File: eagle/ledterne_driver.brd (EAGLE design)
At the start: 100 x 80 mm, 1 part, among them IC1 MEGA8-AI

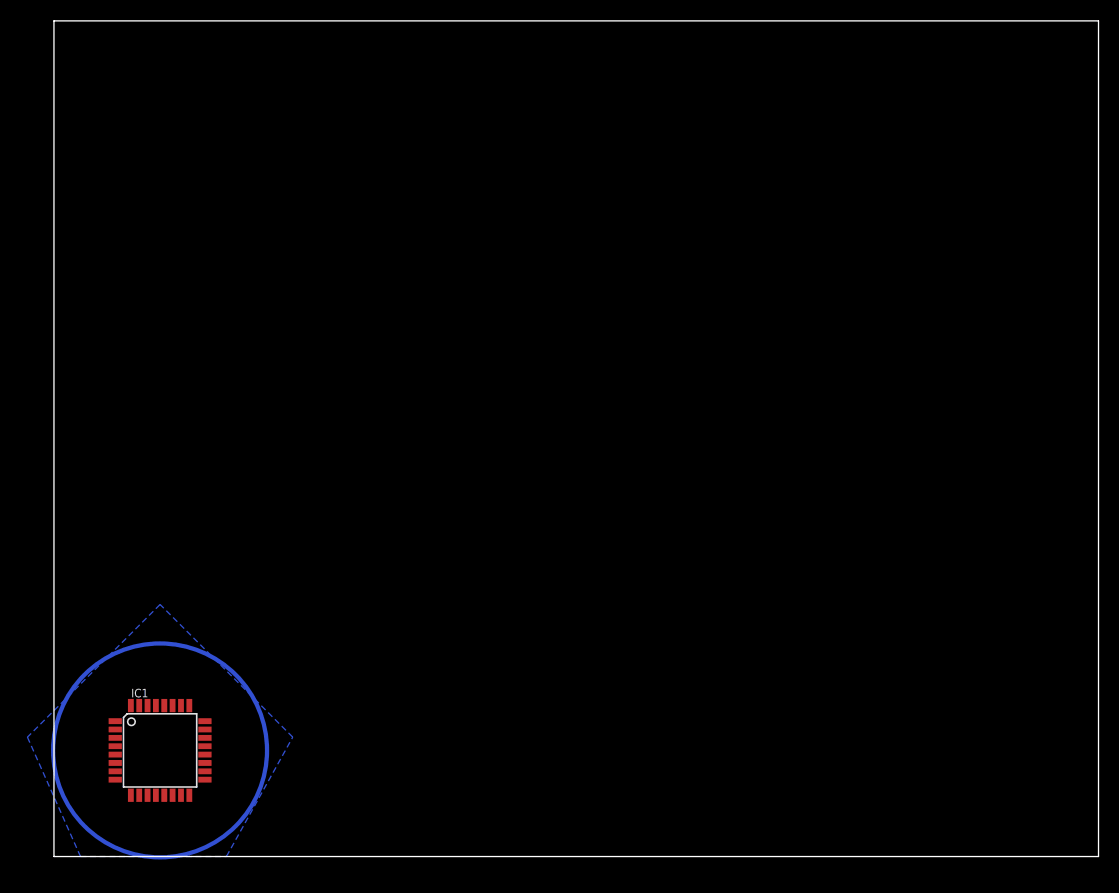
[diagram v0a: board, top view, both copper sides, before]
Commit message: Change driver board to match the display board size
5 display boards will be arranged in an upright position forming
a cylinder with a pentagonal base. The driver board is a pentagon
that then acts as sort of lid for this cylinder.
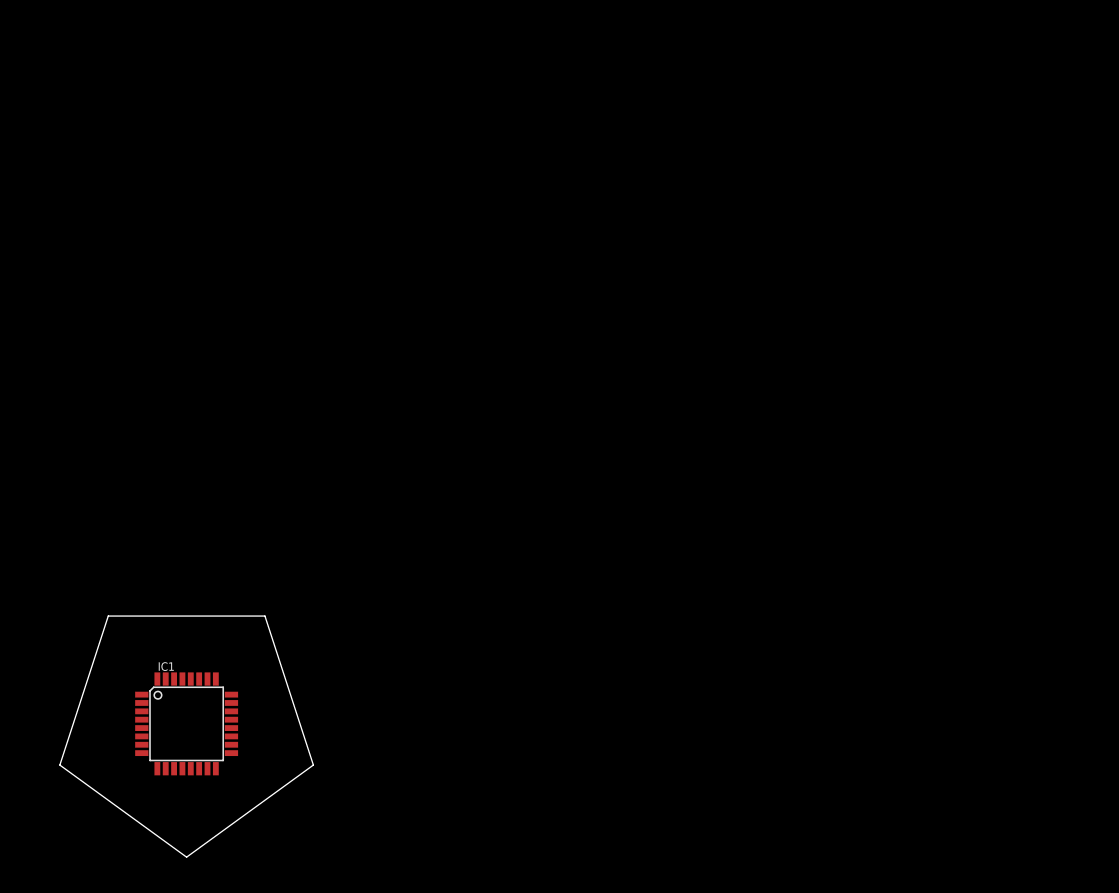
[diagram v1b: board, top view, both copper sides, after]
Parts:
- moved IC1 3.59 mm to (12.7, 12.7)
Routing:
- removed copper zone on layer 16, net N$1
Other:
- board size 100 x 80 mm -> 24.3 x 23.1 mm
- board text added: "15 mm"
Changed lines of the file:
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@@
 <layer number="45" name="Holes" color="7" fill="1" visible="no" active="yes"/>
 <layer number="46" name="Milling" color="3" fill="1" visible="no" active="yes"/>
-<layer number="47" name="Measures" color="7" fill="1" visible="no" active="yes"/>
+<layer number="47" name="Measures" color="7" fill="1" visible="yes" active="yes"/>
 <layer number="48" name="Document" color="7" fill="1" visible="yes" active="yes"/>
 <layer number="49" name="Reference" color="7" fill="1" visible="yes" active="yes"/>
@@
 <board>
 <plain>
-<wire x1="0" y1="0" x2="100" y2="0" width="0" layer="20"/>
-<wire x1="100" y1="0" x2="100" y2="80" width="0" layer="20"/>
-<wire x1="100" y1="80" x2="0" y2="80" width="0" layer="20"/>
-<wire x1="0" y1="80" x2="0" y2="0" width="0" layer="20"/>
-<circle x="10.16" y="10.16" radius="10.239065625" width="0.4064" layer="16"/>
+<circle x="12.7" y="12.7" radius="12.76" width="0.1" layer="49"/>
+<wire x1="12.7" y1="-0.06" x2="24.8353" y2="8.757" width="0.1" layer="20"/>
+<wire x1="24.8353" y1="8.757" x2="20.2" y2="23.0229" width="0.1" layer="20"/>
+<wire x1="20.2" y1="23.0229" x2="5.2" y2="23.0229" width="0.1" layer="20"/>
+<wire x1="5.2" y1="23.0229" x2="0.5647" y2="8.757" width="0.1" layer="20"/>
+<wire x1="0.5647" y1="8.757" x2="12.7" y2="-0.06" width="0.1" layer="20"/>
+<wire x1="20.2" y1="27.94" x2="5.2" y2="27.94" width="0.1" layer="47"/>
+<text x="12.7" y="29.21" size="1.778" layer="47" align="center">15 mm</text>
+<wire x1="5.2" y1="29.21" x2="5.2" y2="26.67" width="0.1" layer="47"/>
+<wire x1="20.2" y1="29.21" x2="20.2" y2="26.67" width="0.1" layer="47"/>
 </plain>
 <attributes>
@@
 </autorouter>
 <elements>
-<element name="IC1" library="atmel" package="TQFP32-08" value="MEGA8-AI" x="10.16" y="10.16">
-<attribute name="OC_NEWARK" value="73M8863" x="10.16" y="10.16" size="1.778" layer="27" display="off"/>
-<attribute name="MF" value="" x="10.16" y="10.16" size="1.778" layer="27" display="off"/>
-<attribute name="OC_FARNELL" value="9171371" x="10.16" y="10.16" size="1.778" layer="27" display="off"/>
-<attribute name="MPN" value="ATMEGA8-16AU" x="10.16" y="10.16" size="1.778" layer="27" display="off"/>
+<element name="IC1" library="atmel" package="TQFP32-08" value="MEGA8-AI" x="12.7" y="12.7">
+<attribute name="OC_NEWARK" value="73M8863" x="12.7" y="12.7" size="1.778" layer="27" display="off"/>
+<attribute name="MF" value="" x="12.7" y="12.7" size="1.778" layer="27" display="off"/>
+<attribute name="OC_FARNELL" value="9171371" x="12.7" y="12.7" size="1.778" layer="27" display="off"/>
+<attribute name="MPN" value="ATMEGA8-16AU" x="12.7" y="12.7" size="1.778" layer="27" display="off"/>
 </element>
 </elements>
@@
 <contactref element="IC1" pad="5"/>
 <contactref element="IC1" pad="21"/>
-<wire x1="5.8674" y1="11.36" x2="5.8674" y2="9.76" width="0" layer="19" extent="1-1"/>
-<wire x1="14.4526" y1="10.56" x2="5.8674" y2="9.76" width="0" layer="19" extent="1-1"/>
+<wire x1="8.4074" y1="13.9" x2="8.4074" y2="12.3" width="0" layer="19" extent="1-1"/>
+<wire x1="16.9926" y1="13.1" x2="8.4074" y2="12.3" width="0" layer="19" extent="1-1"/>
 </signal>
 <signal name="VCC">
 <contactref element="IC1" pad="4"/>
 <contactref element="IC1" pad="6"/>
-<wire x1="5.8674" y1="10.56" x2="5.8674" y2="8.96" width="0" layer="19" extent="1-1"/>
+<wire x1="8.4074" y1="13.1" x2="8.4074" y2="11.5" width="0" layer="19" extent="1-1"/>
 </signal>
 <signal name="AVCC">
 <contactref element="IC1" pad="18"/>
 </signal>
-<signal name="N$1">
-<polygon width="0.4064" layer="16">
-<vertex x="2.54" y="0"/>
-<vertex x="16.51" y="0"/>
-<vertex x="22.86" y="11.43"/>
-<vertex x="10.16" y="24.13"/>
-<vertex x="-2.54" y="11.43"/>
-</polygon>
-</signal>
 </signals>

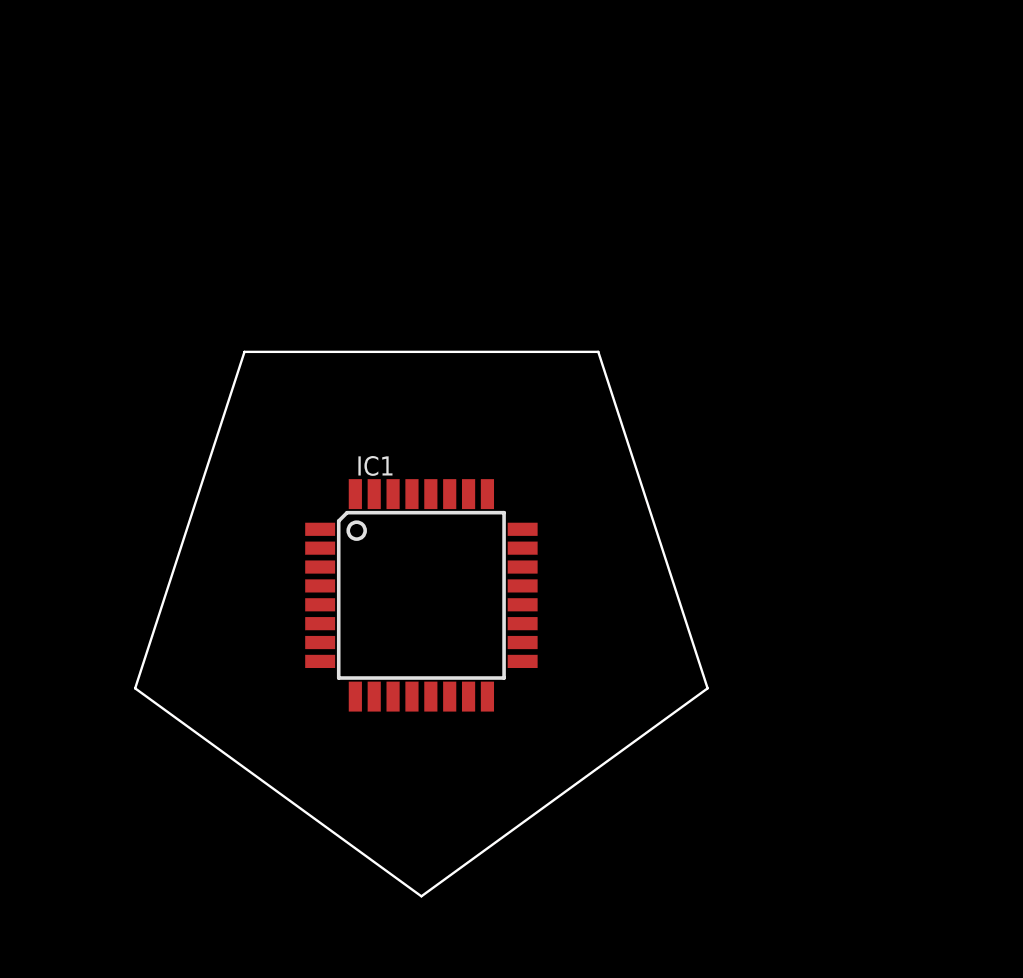
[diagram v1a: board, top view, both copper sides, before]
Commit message: Add connectors to the driver board
These connectors will allow the display boards to attach to the
driver board.

Note that this is just a very rough sketch for demonstrating the
basic idea. The exact placement and type of connectors will have
to be fine-tuned later.
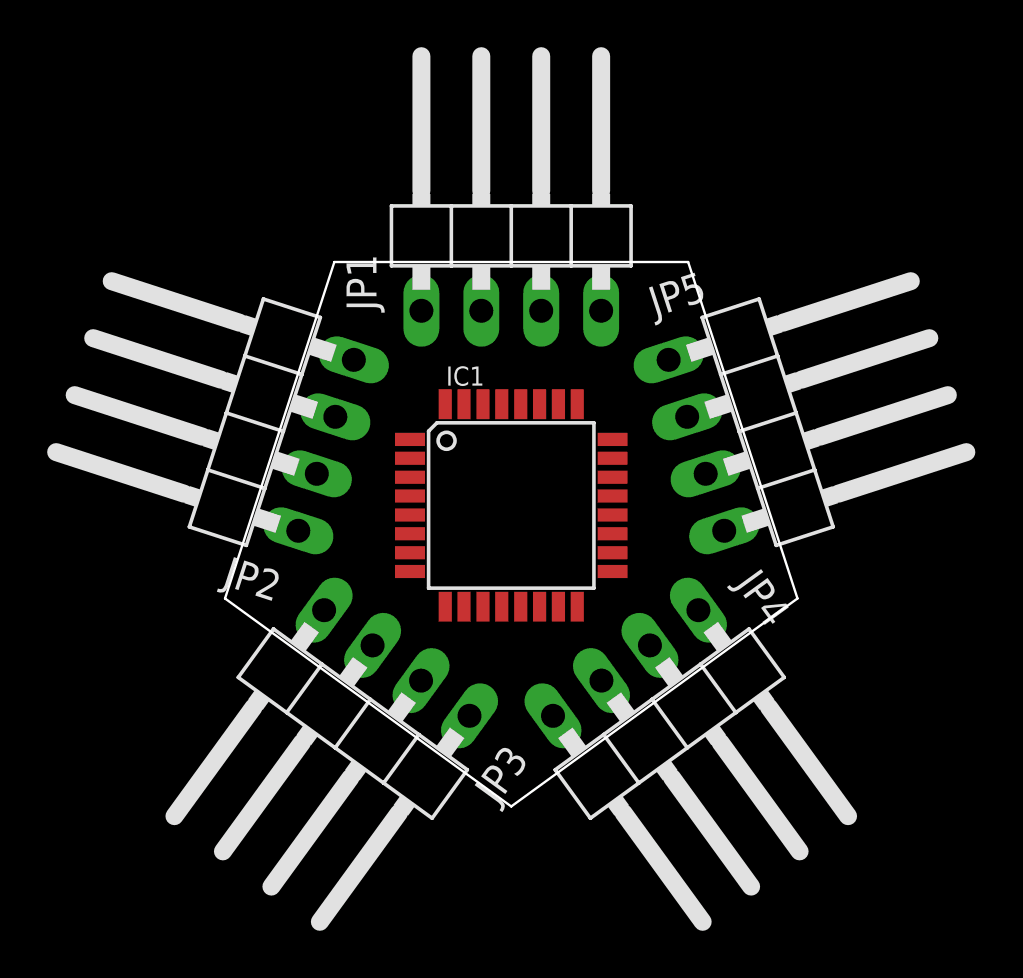
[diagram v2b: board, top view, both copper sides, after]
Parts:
- added JP1, JP2, JP3, JP4, JP5: (no value), pinhead:1X04/90
- moved IC1 5.39 mm to (16.5, 16.5)
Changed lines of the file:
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@@
 <layer number="47" name="Measures" color="7" fill="1" visible="yes" active="yes"/>
 <layer number="48" name="Document" color="7" fill="1" visible="yes" active="yes"/>
-<layer number="49" name="Reference" color="7" fill="1" visible="yes" active="yes"/>
+<layer number="49" name="Reference" color="7" fill="1" visible="no" active="yes"/>
 <layer number="51" name="tDocu" color="7" fill="1" visible="yes" active="yes"/>
 <layer number="52" name="bDocu" color="7" fill="1" visible="yes" active="yes"/>
@@
 <board>
 <plain>
-<circle x="12.7" y="12.7" radius="12.76" width="0.1" layer="49"/>
-<wire x1="12.7" y1="-0.06" x2="24.8353" y2="8.757" width="0.1" layer="20"/>
-<wire x1="24.8353" y1="8.757" x2="20.2" y2="23.0229" width="0.1" layer="20"/>
-<wire x1="20.2" y1="23.0229" x2="5.2" y2="23.0229" width="0.1" layer="20"/>
-<wire x1="5.2" y1="23.0229" x2="0.5647" y2="8.757" width="0.1" layer="20"/>
-<wire x1="0.5647" y1="8.757" x2="12.7" y2="-0.06" width="0.1" layer="20"/>
-<wire x1="20.2" y1="27.94" x2="5.2" y2="27.94" width="0.1" layer="47"/>
-<text x="12.7" y="29.21" size="1.778" layer="47" align="center">15 mm</text>
-<wire x1="5.2" y1="29.21" x2="5.2" y2="26.67" width="0.1" layer="47"/>
-<wire x1="20.2" y1="29.21" x2="20.2" y2="26.67" width="0.1" layer="47"/>
+<circle x="16.51" y="16.51" radius="12.76" width="0.1" layer="49"/>
+<wire x1="16.51" y1="3.75" x2="28.6453" y2="12.567" width="0.1" layer="20"/>
+<wire x1="28.6453" y1="12.567" x2="24.01" y2="26.8329" width="0.1" layer="20"/>
+<wire x1="24.01" y1="26.8329" x2="9.01" y2="26.8329" width="0.1" layer="20"/>
+<wire x1="9.01" y1="26.8329" x2="4.3747" y2="12.567" width="0.1" layer="20"/>
+<wire x1="4.3747" y1="12.567" x2="16.51" y2="3.75" width="0.1" layer="20"/>
+<wire x1="24.01" y1="31.75" x2="9.01" y2="31.75" width="0.1" layer="47"/>
+<text x="16.51" y="33.02" size="1.778" layer="47" align="center">15 mm</text>
+<wire x1="9.01" y1="33.02" x2="9.01" y2="30.48" width="0.1" layer="47"/>
+<wire x1="24.01" y1="33.02" x2="24.01" y2="30.48" width="0.1" layer="47"/>
 </plain>
 <attributes>
@@
 </autorouter>
 <elements>
-<element name="IC1" library="atmel" package="TQFP32-08" value="MEGA8-AI" x="12.7" y="12.7">
-<attribute name="OC_NEWARK" value="73M8863" x="12.7" y="12.7" size="1.778" layer="27" display="off"/>
-<attribute name="MF" value="" x="12.7" y="12.7" size="1.778" layer="27" display="off"/>
-<attribute name="OC_FARNELL" value="9171371" x="12.7" y="12.7" size="1.778" layer="27" display="off"/>
-<attribute name="MPN" value="ATMEGA8-16AU" x="12.7" y="12.7" size="1.778" layer="27" display="off"/>
+<element name="IC1" library="atmel" package="TQFP32-08" value="MEGA8-AI" x="16.51" y="16.51">
+<attribute name="OC_NEWARK" value="73M8863" x="16.51" y="16.51" size="1.778" layer="27" display="off"/>
+<attribute name="MF" value="" x="16.51" y="16.51" size="1.778" layer="27" display="off"/>
+<attribute name="OC_FARNELL" value="9171371" x="16.51" y="16.51" size="1.778" layer="27" display="off"/>
+<attribute name="MPN" value="ATMEGA8-16AU" x="16.51" y="16.51" size="1.778" layer="27" display="off"/>
 </element>
+<element name="JP1" library="pinhead" package="1X04/90" value="" x="16.51" y="28.575"/>
+<element name="JP2" library="pinhead" package="1X04/90" value="" x="5.0355" y="20.238" rot="R72"/>
+<element name="JP3" library="pinhead" package="1X04/90" value="" x="9.4184" y="6.7492" rot="R144"/>
+<element name="JP4" library="pinhead" package="1X04/90" value="" x="23.6016" y="6.7492" rot="R216"/>
+<element name="JP5" library="pinhead" package="1X04/90" value="" x="27.984" y="20.238" rot="R288"/>
 </elements>
 <signals>
@@
 <contactref element="IC1" pad="5"/>
 <contactref element="IC1" pad="21"/>
-<wire x1="8.4074" y1="13.9" x2="8.4074" y2="12.3" width="0" layer="19" extent="1-1"/>
-<wire x1="16.9926" y1="13.1" x2="8.4074" y2="12.3" width="0" layer="19" extent="1-1"/>
+<wire x1="12.2174" y1="17.71" x2="12.2174" y2="16.11" width="0" layer="19" extent="1-1"/>
+<wire x1="20.8026" y1="16.91" x2="12.2174" y2="16.11" width="0" layer="19" extent="1-1"/>
 </signal>
 <signal name="VCC">
 <contactref element="IC1" pad="4"/>
 <contactref element="IC1" pad="6"/>
-<wire x1="8.4074" y1="13.1" x2="8.4074" y2="11.5" width="0" layer="19" extent="1-1"/>
+<wire x1="12.2174" y1="16.91" x2="12.2174" y2="15.31" width="0" layer="19" extent="1-1"/>
 </signal>
 <signal name="AVCC">

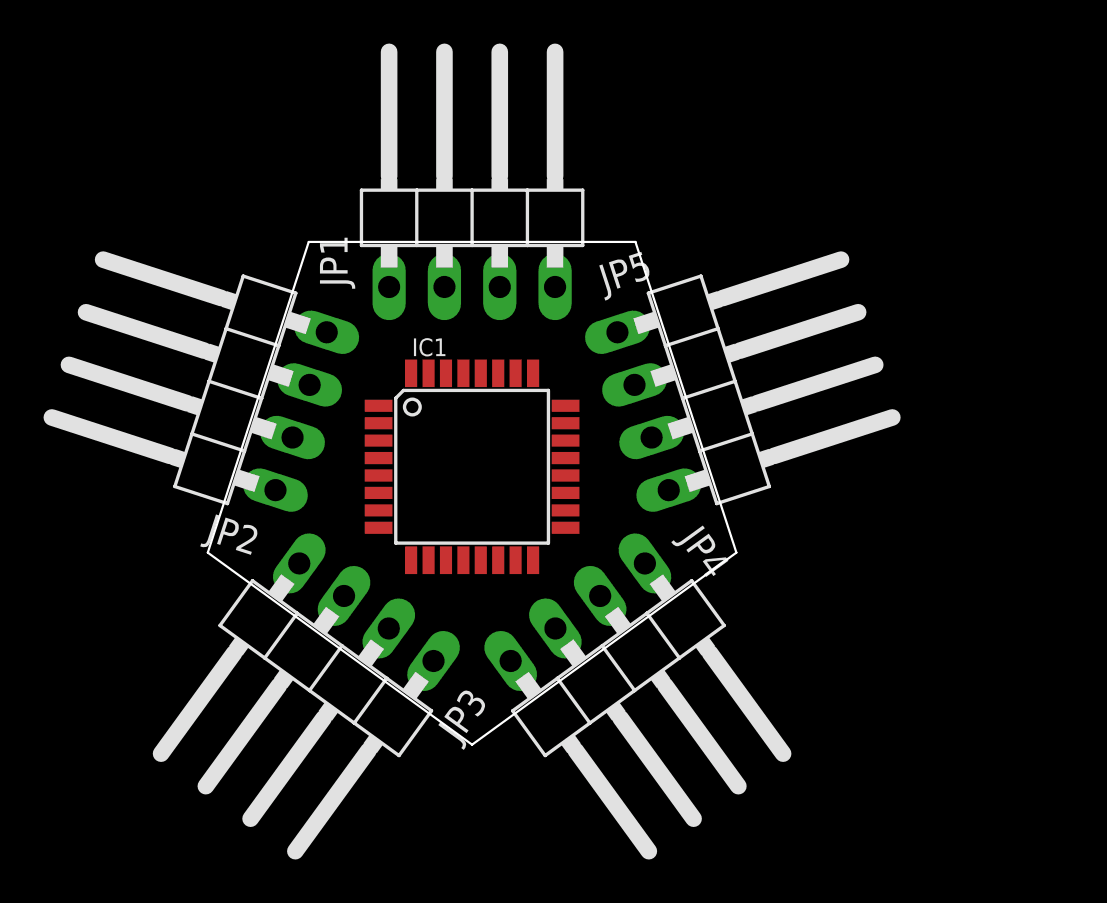
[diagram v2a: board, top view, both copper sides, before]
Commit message: Start connecting the components of the driver.
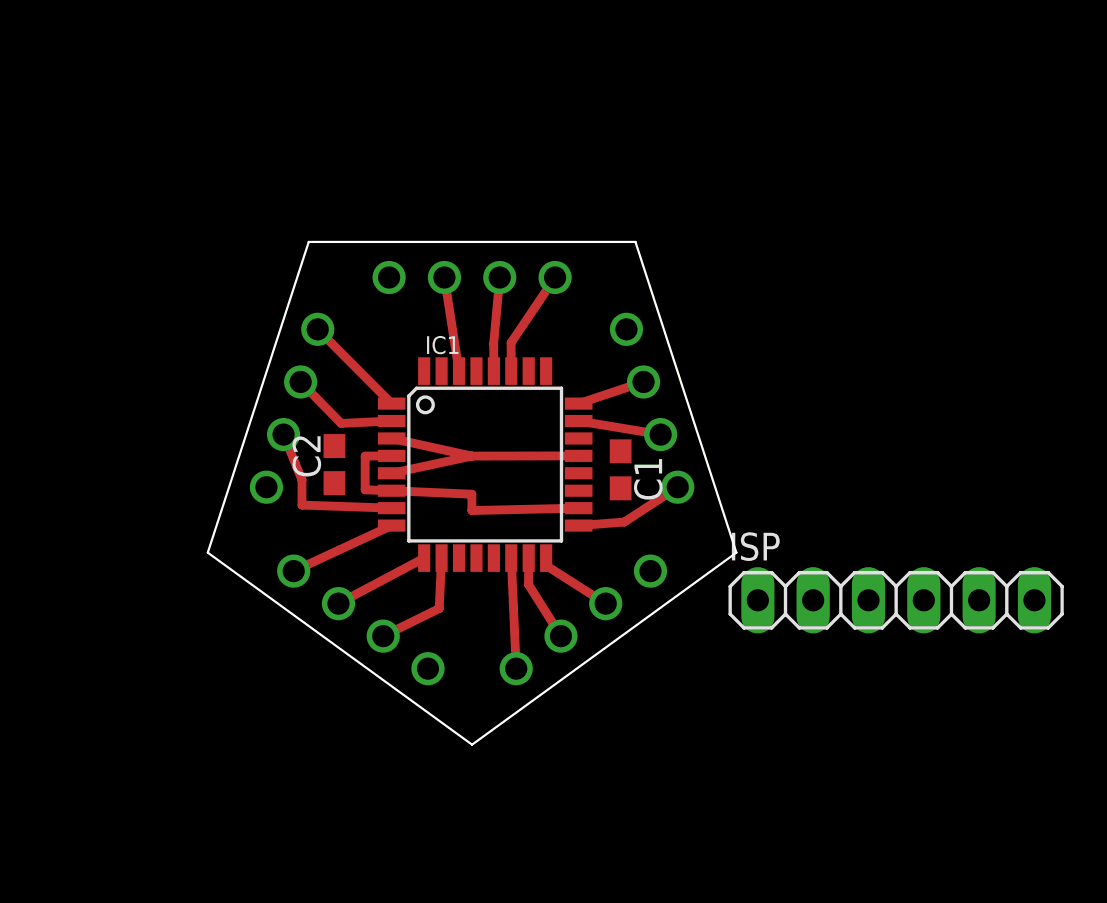
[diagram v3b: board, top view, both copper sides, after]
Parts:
- added C1, C2: (no value), rcl:C0603
- added ISP: (no value), pinhead:1X06
- JP1, JP2, JP3, JP4, JP5: device pinhead:1X04/90 -> pinhead_round_pads:1X04/90
- moved JP2 23.4 mm to (28.4, 20.4), flipped to the bottom
- moved JP5 23.4 mm to (4.62, 20.4), flipped to the bottom
- moved JP4 14.4 mm to (9.16, 6.40), flipped to the bottom
- moved JP3 14.4 mm to (23.9, 6.40), flipped to the bottom
- moved IC1 0.61 mm to (17.1, 16.6)
- moved JP1 0.44 mm to (16.5, 29.0), flipped to the bottom
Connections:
- removed net AVCC: IC1.18
- new net MISO: IC1.16, ISP.3, JP3.3
- new net MOSI: IC1.15, ISP.4, JP3.2
- new net N$1: C1.2, IC1.20
- new net N$10: IC1.10, JP4.3
- new net N$11: IC1.7, JP5.3
- new net N$12: IC1.8, JP4.1
- new net N$13: IC1.1, JP5.1
- new net N$2: IC1.30, JP1.3
- new net N$3: IC1.28, JP1.2
- new net N$4: IC1.27, JP1.1
- new net N$5: IC1.23, JP2.2
- new net N$6: IC1.2, JP5.2
- new net N$7: IC1.24, JP2.3
- new net N$8: IC1.14, JP3.1
- new net N$9: IC1.9, JP4.2
- new net RESET: IC1.29, ISP.5
- new net SCK: IC1.17, ISP.2, JP2.1
- net GND: now also C1.1, C2.2, ISP.1, JP1.4, JP2.4, JP3.4, JP4.4, JP5.4
- net VCC: now also C2.1, IC1.18, ISP.6
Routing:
- net VCC: track 0.00 -> 13.3 mm
- net GND: track 0.00 -> 12.4 mm
- net N$11: track 0.00 -> 7.52 mm
- net N$10: track 0.00 -> 5.19 mm
- net N$8: track 0.00 -> 5.08 mm
- net SCK: track 0.00 -> 5.03 mm
- net N$6: track 0.00 -> 4.98 mm
- net N$12: track 0.00 -> 4.96 mm
- net N$4: track 0.00 -> 4.91 mm
- net N$13: track 0.00 -> 4.81 mm
- net N$9: track 0.00 -> 4.46 mm
- net N$2: track 0.00 -> 4.35 mm
- net N$3: track 0.00 -> 4.31 mm
- net MOSI: track 0.00 -> 4.01 mm
- net N$5: track 0.00 -> 3.82 mm
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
